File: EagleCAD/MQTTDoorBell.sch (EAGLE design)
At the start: 17 parts, among them Q1 MMBT2222

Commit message: updating design and starting to structure board
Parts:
- removed C4: (no value), adafruit:CPOL-USE5-13
- U$1: SPICEPREFIX (none) -> B
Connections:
- removed net BELL_OUT1: J1.5
- net 16V_AC1: now also J1.5
- net 16V_AC2: now also U$1G$1.P
- net 3.3V: no longer C4.+
- net BELL_OUT2: now also U$1G$1.S
- net BUTTON1: now also X1.GPIO16
- net GND: no longer C4.-
- net RELAYSIGNAL: now also X1.GPIO0

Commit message: initial commit of eagle files, version 1 of board'
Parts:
- removed C3: (no value), adafruit:CPOL-USE5-13
- removed J1: (no value), SparkFun-Connectors:CONN_063.5MM-6
- removed JP1: (no value), adafruit:PINHD-1X3CB
- added C4: 10uf, SparkFun-Capacitors:10UF-0805-10V-10%
- added C7: (no value), adafruit:CPOL-USE5-10.5
- added J2: (no value), SparkFun-Connectors:CONN_023.5MM
- added J3: (no value), SparkFun-Connectors:CONN_04SCREW
- added PROG: (no value), SparkFun-Connectors:CONN_05
- added R6, R7: 2K, microbuilder:RESISTOR0805_NOOUTLINE
- added SW2: SPST_TACT-EVQQ2, adafruit:SPST_TACT-EVQQ2
- added U1: TSR_1-2433, Traco_TSR:TSR_1-2433
- R1, R2, R3: value (none) -> 10k
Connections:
- removed net BUTTON2: J1.4
- new net GPIO0: PROG.2, X1.GPIO0
- new net RELAYDETECT: R6.2, X1.GPIO5
- new net RESET: R7.1, SW2.S, SW2.S1, X1.RESET
- net 16V_AC1: now also J3.1; no longer J1.1, J1.5
- net 16V_AC2: now also J3.2, J3.3; no longer J1.2
- net 16V_DC: now also C7.+, U1.VI; no longer C3.+, JP1.1
- net 3.3V: now also C4.1, J2.1, PROG.1, R7.2, U1.VO; no longer JP1.3
- net BELL_OUT2: now also J3.4; no longer J1.6
- net BUTTON1: no longer J1.3
- net GND: now also C4.2, C7.-, PROG.5, SW2.P, SW2.P1, U1.GND; no longer C3.-, JP1.2
- net GPIO15: now also X1.GPIO15
- net GPIO2: now also X1.GPIO2
- net RELAYSIGNAL: now also J2.2, R6.1; no longer X1.GPIO0
- net RX: now also PROG.3
- net TX: now also PROG.4

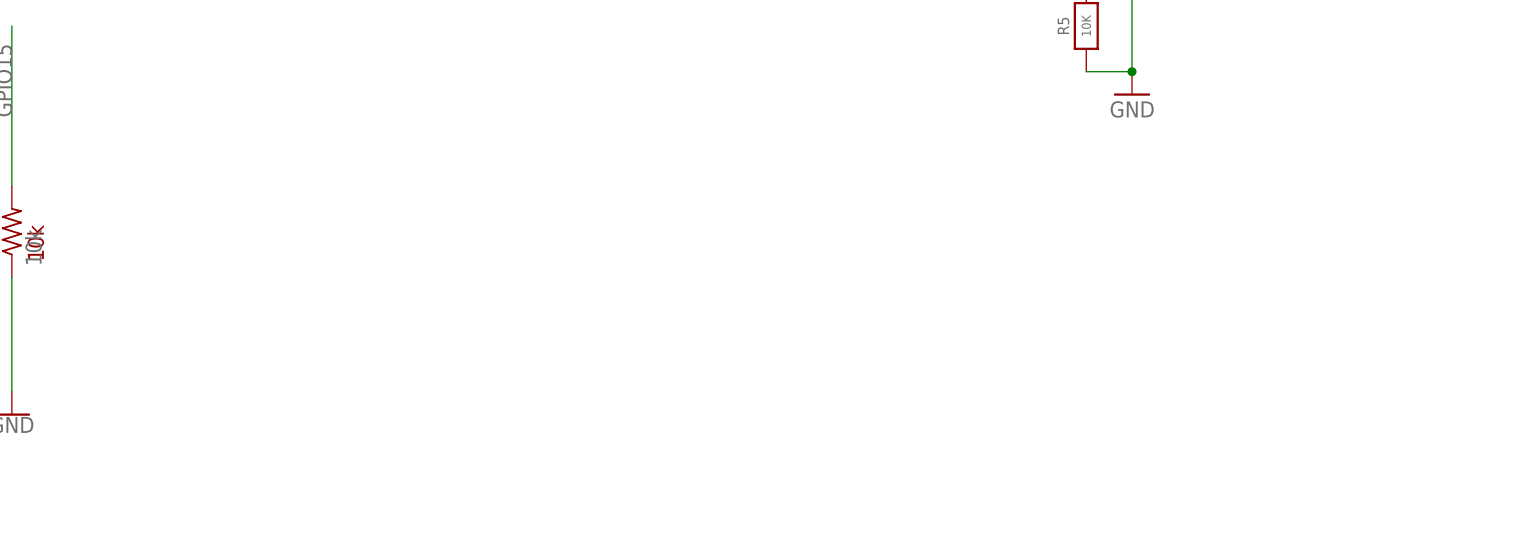
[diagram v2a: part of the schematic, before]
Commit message: fix polygon issue and add labels'
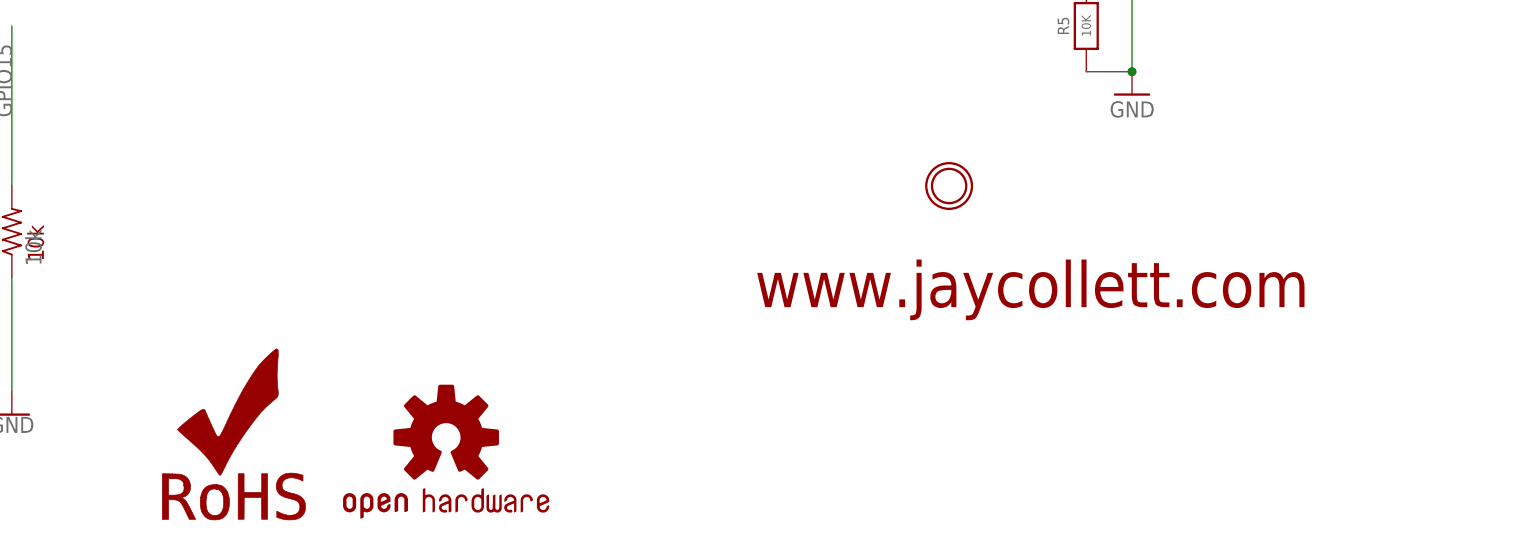
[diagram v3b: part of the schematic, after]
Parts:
- added LOGO1: OSHW-LOGOMINI, SparkFun-Aesthetics:OSHW-LOGOMINI
- added LOGO2: ROHS_LOGO, SparkFun-Aesthetics:ROHS_LOGO
- added U$4: MICROBUILDER_MOUNTINGHOLE3.0THIN, microbuilder:MICROBUILDER_MOUNTINGHOLE3.0THIN
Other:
- note added: "www.jaycollett.com"

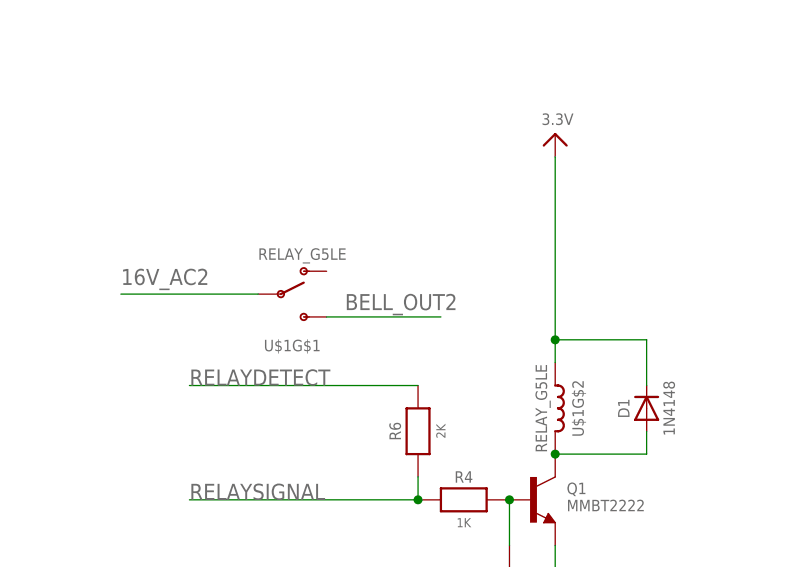
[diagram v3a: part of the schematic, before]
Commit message: add new PCB board and schematic, add first draf of firmware
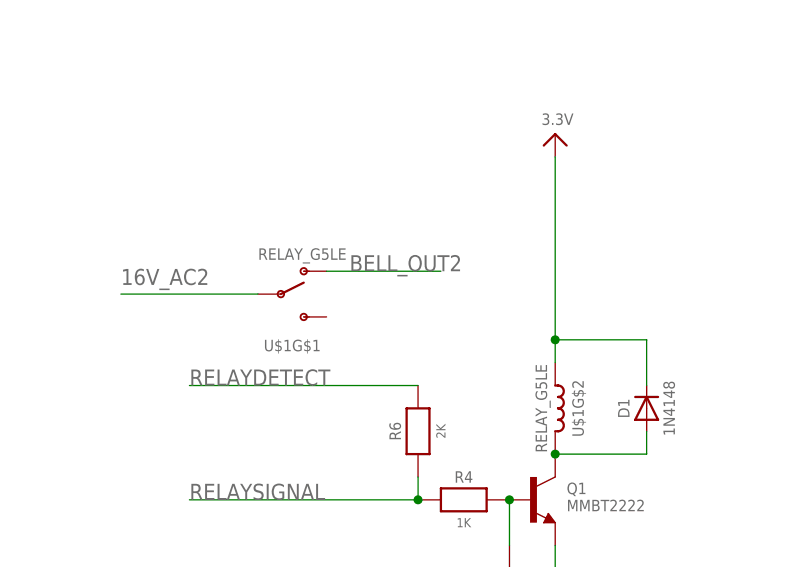
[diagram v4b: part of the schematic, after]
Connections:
- net BELL_OUT2: now also U$1G$1.O; no longer U$1G$1.S

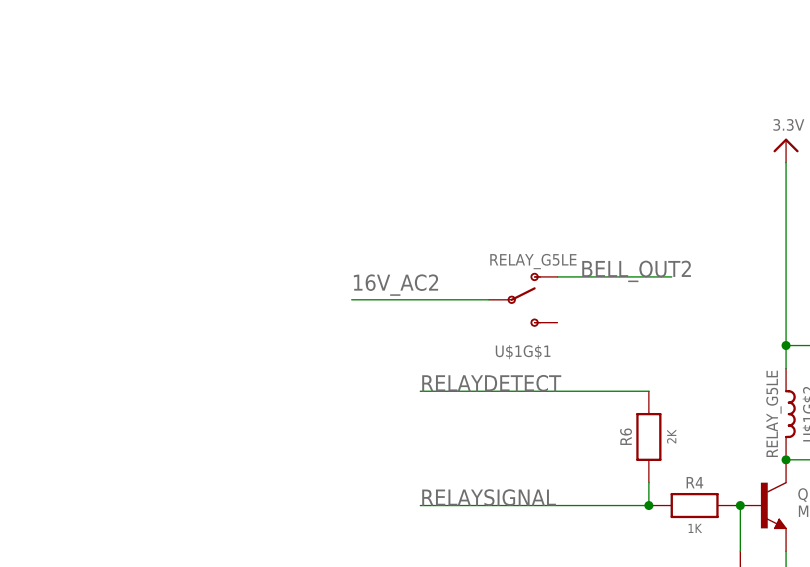
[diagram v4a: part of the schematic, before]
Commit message: fixing critical error with AC power lines to doorbell ringer
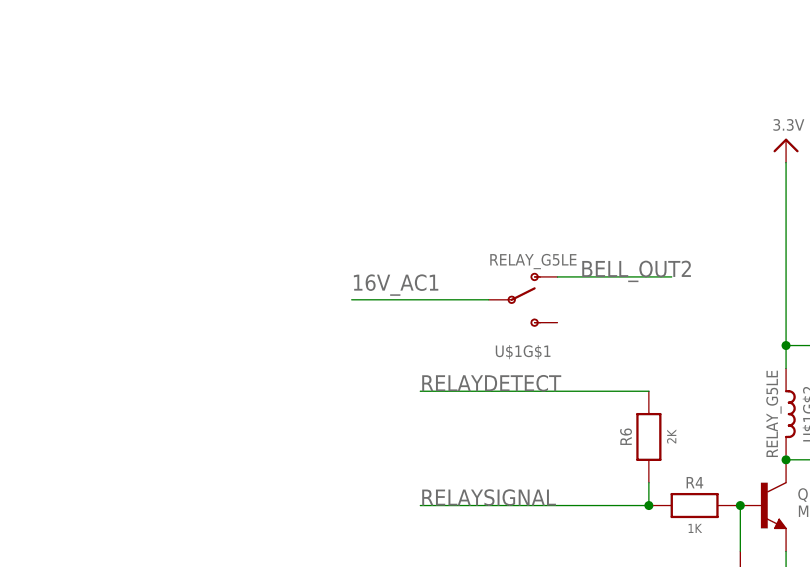
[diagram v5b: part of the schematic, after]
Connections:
- net 16V_AC1: now also U$1G$1.P
- net 16V_AC2: no longer U$1G$1.P
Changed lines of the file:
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@@
-</segment>
-<segment>
-<pinref part="U$1" gate="G$1" pin="P"/>
-<wire x1="175.26" y1="91.44" x2="160.02" y2="91.44" width="0.1524" layer="91"/>
-<label x="160.02" y="92.456" size="1.778" layer="95"/>
 </segment>
 <segment>
@@
 <label x="30.48" y="172.72" size="1.778" layer="95"/>
 </segment>
+<segment>
+<pinref part="U$1" gate="G$1" pin="P"/>
+<wire x1="175.26" y1="91.44" x2="160.02" y2="91.44" width="0.1524" layer="91"/>
+<label x="160.02" y="92.456" size="1.778" layer="95"/>
+</segment>
 </net>
